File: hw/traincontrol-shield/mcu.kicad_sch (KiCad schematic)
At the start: 7 parts, among them J1 ESP32-S3 Header L, J2 ESP32-S3 Header R

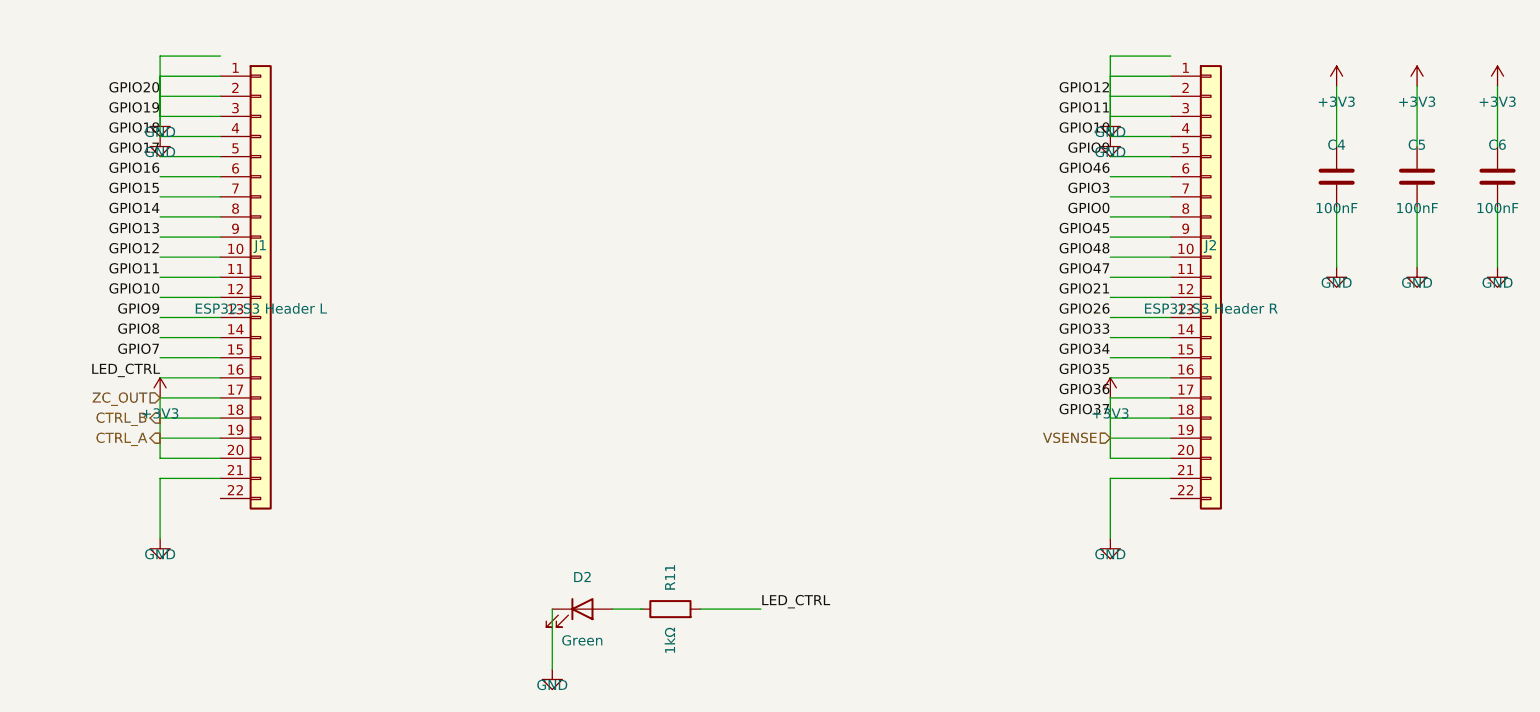
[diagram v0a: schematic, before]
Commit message: Fix schematic ERC errors: pin Y-flip, PWR_FLAG, label wiring, spacing
- Fix connector pin positions using Y-flip convention (sym Y-up → sch Y-down)
- Add GND PWR_FLAG to power-supply sheet (eliminates power_pin_not_driven)
- Fix top-level connector label placement: labels at stub end, wires toward pins
- Apply omnidirectional spacing and IC-to-passive body gap rules across sheets
- Update schematics-plan.md with ERC workflow and coordinate conventions
- Regenerate all sub-sheets with corrected generator scripts

ERC result: 138 violations (all warnings/cosmetic), 0 critical errors.

Co-Authored-By: Claude Opus 4.6 <noreply@anthropic.com>
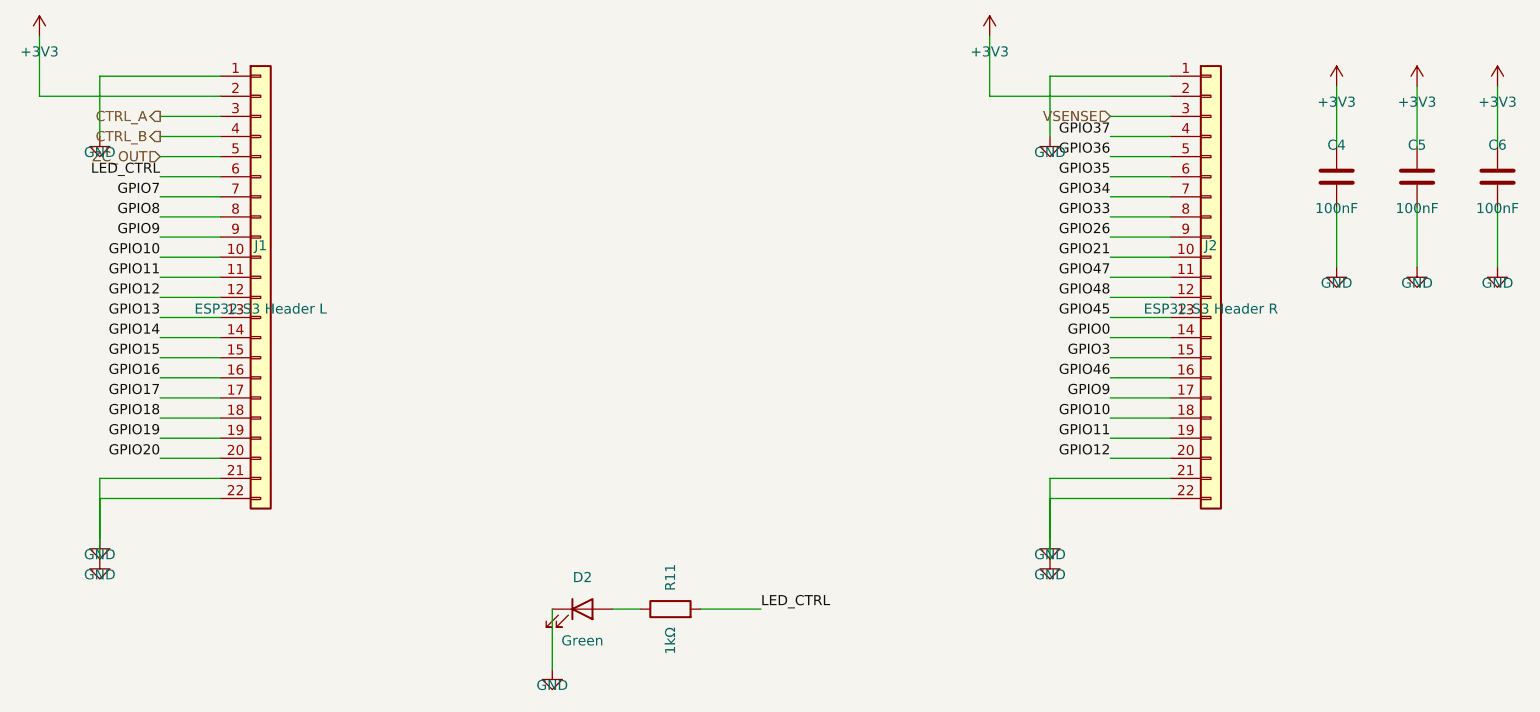
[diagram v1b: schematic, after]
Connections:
- net +3V3: now also J1.2 (Pin_2), J2.2 (Pin_2); no longer J1.17 (Pin_17), J1.18 (Pin_18), J1.19 (Pin_19), J1.20 (Pin_20), J2.17 (Pin_17), J2.18 (Pin_18), J2.19 (Pin_19), J2.20 (Pin_20)
- net GND: now also J1.22 (Pin_22), J2.22 (Pin_22); no longer J1.10 (Pin_10), J1.11 (Pin_11), J1.12 (Pin_12), J1.2 (Pin_2), J1.3 (Pin_3), J1.4 (Pin_4), J2.2 (Pin_2), J2.3 (Pin_3), J2.4 (Pin_4)
- net GPIO0: now also J2.14 (Pin_14); no longer J2.8 (Pin_8)
- net GPIO13: now also J1.13 (Pin_13); no longer J1.9 (Pin_9)
- net GPIO14: now also J1.14 (Pin_14); no longer J1.8 (Pin_8)
- net GPIO15: now also J1.15 (Pin_15); no longer J1.7 (Pin_7)
- net GPIO16: now also J1.16 (Pin_16); no longer J1.6 (Pin_6)
- net GPIO17: now also J1.17 (Pin_17); no longer J1.5 (Pin_5)
- net GPIO21: now also J2.10 (Pin_10); no longer J2.12 (Pin_12)
- net GPIO26: now also J2.9 (Pin_9); no longer J2.13 (Pin_13)
- net GPIO3: now also J2.15 (Pin_15); no longer J2.7 (Pin_7)
- net GPIO33: now also J2.8 (Pin_8); no longer J2.14 (Pin_14)
- net GPIO34: now also J2.7 (Pin_7); no longer J2.15 (Pin_15)
- net GPIO35: now also J2.6 (Pin_6); no longer J2.16 (Pin_16)
- net GPIO45: now also J2.13 (Pin_13); no longer J2.9 (Pin_9)
- net GPIO46: now also J2.16 (Pin_16); no longer J2.6 (Pin_6)
- net GPIO48: now also J2.12 (Pin_12); no longer J2.10 (Pin_10)
- net GPIO7: now also J1.7 (Pin_7); no longer J1.15 (Pin_15)
- net GPIO8: now also J1.8 (Pin_8); no longer J1.14 (Pin_14)
- net GPIO9: now also J1.9 (Pin_9), J2.17 (Pin_17); no longer J1.13 (Pin_13), J2.5 (Pin_5)
- net LED_CTRL: now also J1.6 (Pin_6); no longer J1.16 (Pin_16)
- net at D2.2 (A): now also R11.1
- new net CTRL_A: J1.3 (Pin_3)
- new net CTRL_B: J1.4 (Pin_4)
- new net GPIO10: J1.10 (Pin_10), J2.18 (Pin_18)
- new net GPIO11: J1.11 (Pin_11), J2.19 (Pin_19)
- new net GPIO12: J1.12 (Pin_12), J2.20 (Pin_20)
- new net GPIO18: J1.18 (Pin_18)
- new net GPIO19: J1.19 (Pin_19)
- new net GPIO20: J1.20 (Pin_20)
- new net GPIO36: J2.5 (Pin_5)
- new net GPIO37: J2.4 (Pin_4)
- new net VSENSE: J2.3 (Pin_3)
- new net ZC_OUT: J1.5 (Pin_5)
